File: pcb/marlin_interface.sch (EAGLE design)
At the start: 8 parts

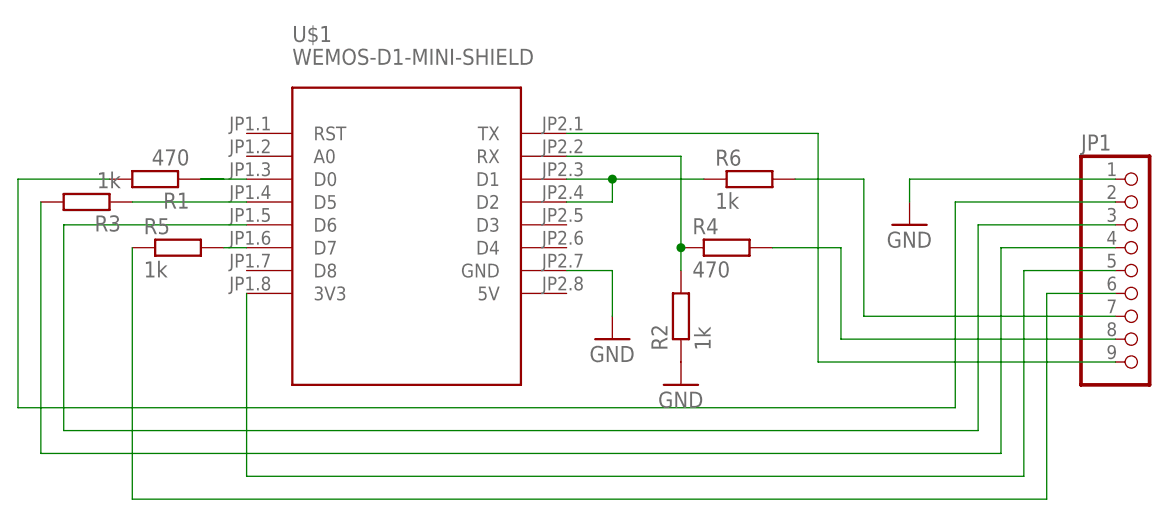
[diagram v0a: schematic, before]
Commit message: remove auto mode from sd
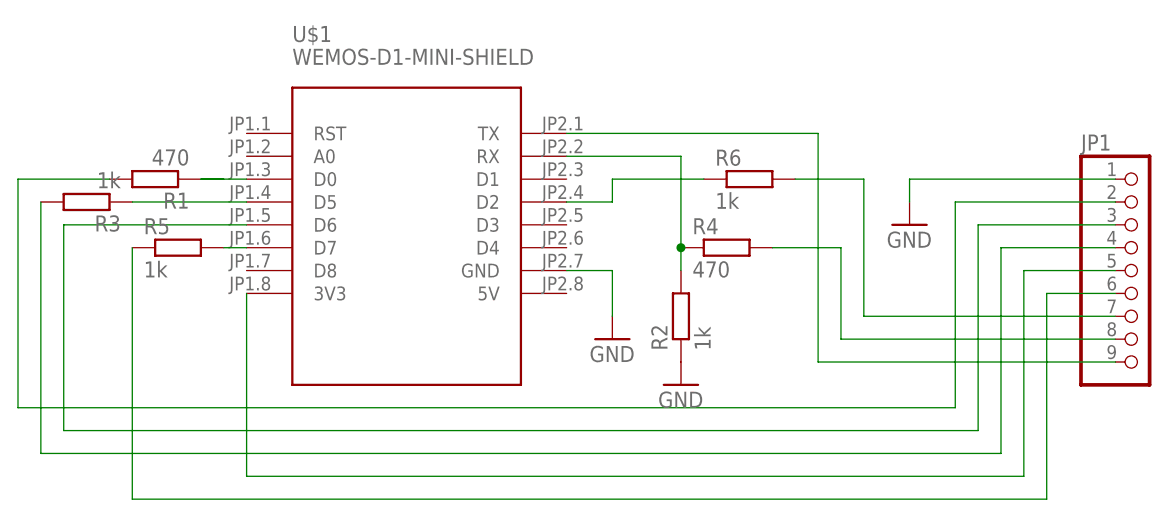
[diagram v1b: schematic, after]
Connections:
- net N$12: no longer U$1.D1
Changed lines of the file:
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@@
 <?xml version="1.0" encoding="utf-8"?>
 <!DOCTYPE eagle SYSTEM "eagle.dtd">
-<eagle version="9.5.2">
+<eagle version="9.6.0">
 <drawing>
 <settings>
@@
 <net name="N$12" class="0">
 <segment>
-<pinref part="U$1" gate="G$1" pin="D1"/>
 <pinref part="R6" gate="G$1" pin="1"/>
-<wire x1="20.32" y1="83.82" x2="25.4" y2="83.82" width="0.1524" layer="91"/>
 <wire x1="25.4" y1="83.82" x2="35.56" y2="83.82" width="0.1524" layer="91"/>
 <pinref part="U$1" gate="G$1" pin="D2"/>
 <wire x1="20.32" y1="81.28" x2="25.4" y2="81.28" width="0.1524" layer="91"/>
 <wire x1="25.4" y1="81.28" x2="25.4" y2="83.82" width="0.1524" layer="91"/>
-<junction x="25.4" y="83.82"/>
-</segment>
-</net>
+</segment>
+</net>
